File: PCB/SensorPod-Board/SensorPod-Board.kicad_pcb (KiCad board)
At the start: 2 copper layers, 67.9 x 92.1 mm, 16 parts, among them J1 Board Header, J2 EXT I2C, J3 Reset, J4 Backup DC, U1 Pico W, U2 SCD30, U3 LM1117-3.3

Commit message: Board fixes
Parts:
- moved U2 0.22 mm to (106.0, 106.3)
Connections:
- U1 pad 4: unconnected-(U1-Pad4) -> Net-(J2-Pad3)
- U1 pad 5: Net-(J2-Pad3) -> Net-(J2-Pad2)
- U1 pad 6: unconnected-(U1-Pad6) -> Net-(U1-Pad6)
- U1 pad 7: unconnected-(U1-Pad7) -> Net-(U1-Pad7)
- U1 pad 9: Net-(J2-Pad2) -> unconnected-(U1-Pad9)
- U2 pad 3: Net-(J2-Pad3) -> Net-(U1-Pad7)
- U2 pad 4: Net-(J2-Pad2) -> Net-(U1-Pad6)
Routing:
- net Net-(U1-Pad6): track 0.00 -> 26.5 mm
- net Net-(U1-Pad7): track 0.00 -> 14.2 mm
- net Net-(J2-Pad2): track 67.6 -> 79.3 mm
- net Net-(J2-Pad3): track 67.1 -> 74.3 mm

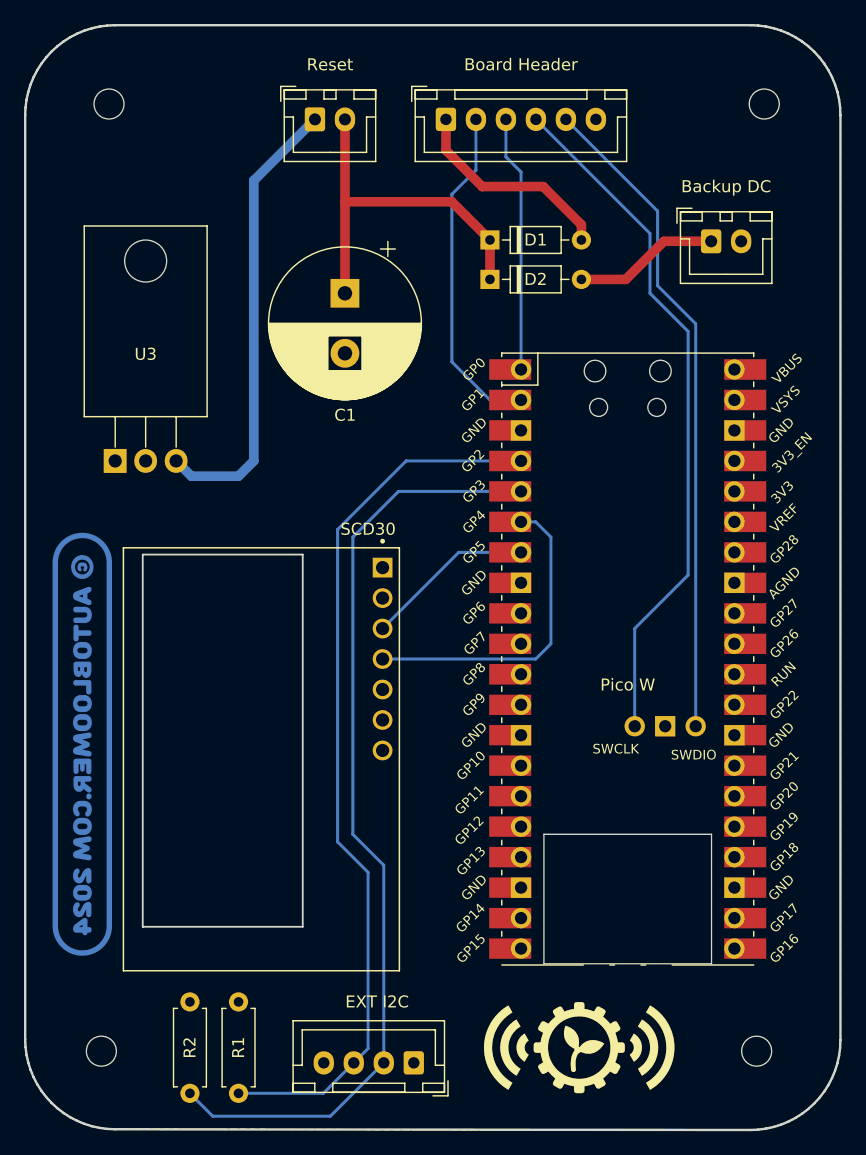
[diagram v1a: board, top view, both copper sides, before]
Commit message: Better board version. Power cycling of sensor controlled by Pico.
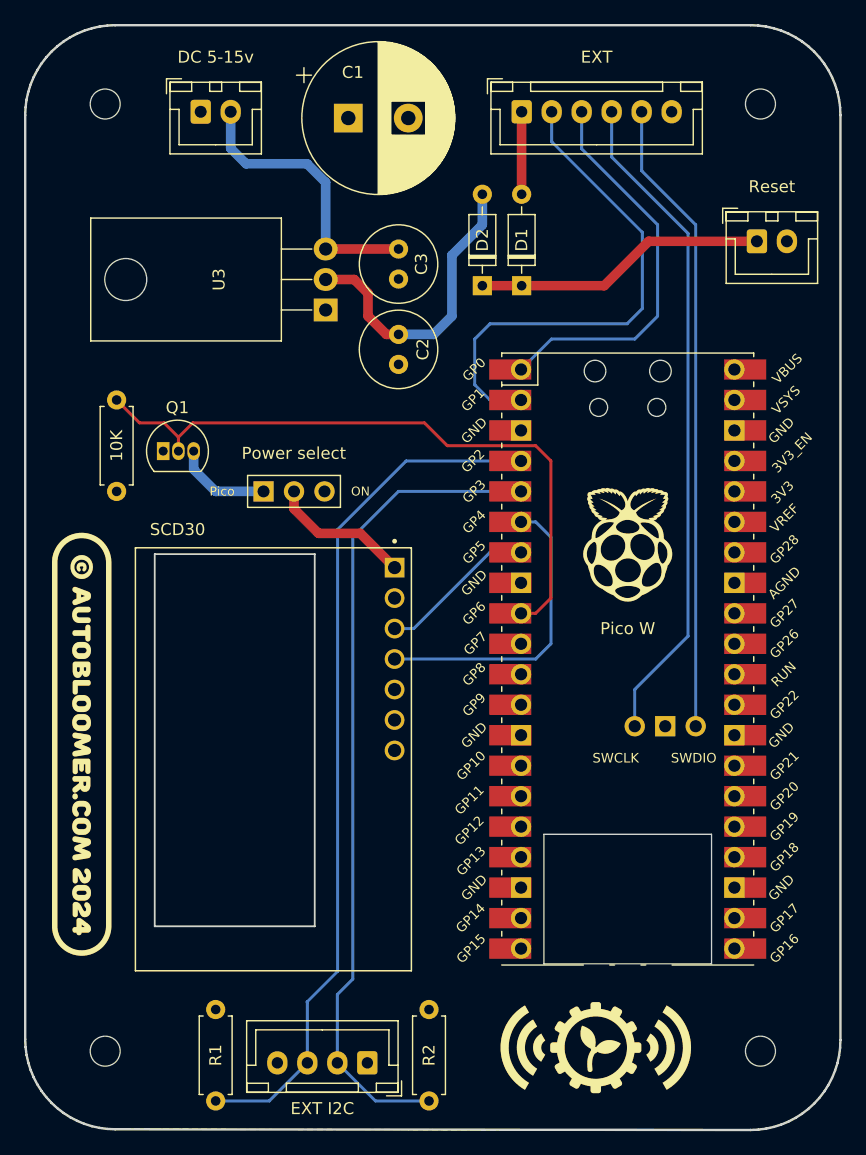
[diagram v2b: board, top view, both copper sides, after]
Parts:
- added C2: 10uF, Capacitor_THT:C_Radial_D6.3mm_H5.0mm_P2.50mm, F.Cu at (117.5, 70.7)
- added C3: 10uF, Capacitor_THT:C_Radial_D6.3mm_H5.0mm_P2.50mm, F.Cu at (117.5, 63.6)
- added J5: Power select, Connector_PinHeader_2.54mm:PinHeader_1x03_P2.54mm_Vertical, F.Cu at (106.2, 83.8)
- added Q1: TP0610L, Package_TO_SOT_THT:TO-92L_Inline, F.Cu at (97.9, 80.5)
- added R3: 10K, Resistor_THT:R_Axial_DIN0207_L6.3mm_D2.5mm_P7.62mm_Horizontal, F.Cu at (94.0, 83.8)
- C1: value 10000uF -> 1000uF
- J1: value Board Header -> EXT
- J4: value Backup DC -> DC 5-15v
- moved J4 43.9 mm to (101.0, 52.2)
- moved J3 38.2 mm to (147.3, 63.0)
- moved U3 21.6 mm to (111.4, 68.7), turned to 90 degrees
- moved R2 19.9 mm to (120.0, 127.0)
- moved C1 14.6 mm to (113.3, 52.7), turned to 0 degrees
- moved J1 6.34 mm to (127.7, 52.2)
- moved D1 4.64 mm to (127.7, 66.7), turned to 90 degrees
- moved J2 3.87 mm to (114.9, 131.4)
- moved R1 2.01 mm to (102.2, 127.0)
- moved U2 1.00 mm to (107.0, 106.3)
- moved D2 0.82 mm to (124.5, 66.7), turned to 90 degrees
- moved REF** 0.32 mm to (147.6, 51.5)
- moved REF** 0.32 mm to (93.0, 130.5)
- moved REF** 0.32 mm to (93.0, 51.5)
- moved REF** 0.32 mm to (147.6, 130.5)
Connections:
- C1 pad 1: +5V -> +3.3V
- D1 pad 1: +5V -> Net-(D1-Pad1)
- D2 pad 1: +5V -> Net-(D1-Pad1)
- D2 pad 2: Net-(D2-Pad2) -> Net-(C2-Pad1)
- J3 pad 1: Net-(J3-Pad1) -> Net-(D1-Pad1)
- J3 pad 2: +5V -> +3.3V
- J4 pad 1: Net-(D2-Pad2) -> GND
- J4 pad 2: GND -> Net-(C3-Pad1)
- U1 pad 9: unconnected-(U1-Pad9) -> Net-(Q1-Pad2)
- U2 pad 1: +3.3V -> Net-(J5-Pad2)
- U3 pad 2: +3.3V -> Net-(C2-Pad1)
- U3 pad 3: Net-(J3-Pad1) -> Net-(C3-Pad1)
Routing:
- net Net-(Q1-Pad2): track 0.00 -> 54.9 mm
- net Net-(J3-Pad1): track 38.1 -> 0.00 mm
- net +5V: track 31.2 -> 0.00 mm
- net Net-(C2-Pad1): track 0.00 -> 25.4 mm
- net Net-(D1-Pad1): track 0.00 -> 24.4 mm
- net Net-(C3-Pad1): track 0.00 -> 23.8 mm
- net Net-(J1-Pad2): track 28.1 -> 42.8 mm
- net Net-(D2-Pad2): track 12.1 -> 0.00 mm
- net Net-(J5-Pad2): track 0.00 -> 11.9 mm
- net Net-(J1-Pad3): track 21.4 -> 32.9 mm
- net Net-(J1-Pad1): track 17.7 -> 6.88 mm
- net Net-(J2-Pad2): track 79.3 -> 68.9 mm
- net Net-(J5-Pad1): track 0.00 -> 8.11 mm
- net Net-(J2-Pad3): track 74.3 -> 72.1 mm
- net Net-(J1-Pad5): track 55.1 -> 53.1 mm
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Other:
- outline, holes or cut-outs redrawn
- board text added: "ON"
- board text added: "Pico"
